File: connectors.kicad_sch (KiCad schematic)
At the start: 15 parts, among them J10 Conn_01x03_Socket, J11 Conn_01x05_Socket, J2 RJ45_RB1-125B8G1A, J6 Conn_01x04_Socket, J8 87832-1420, Q1 MMBT3904, Q2 MMBT3904

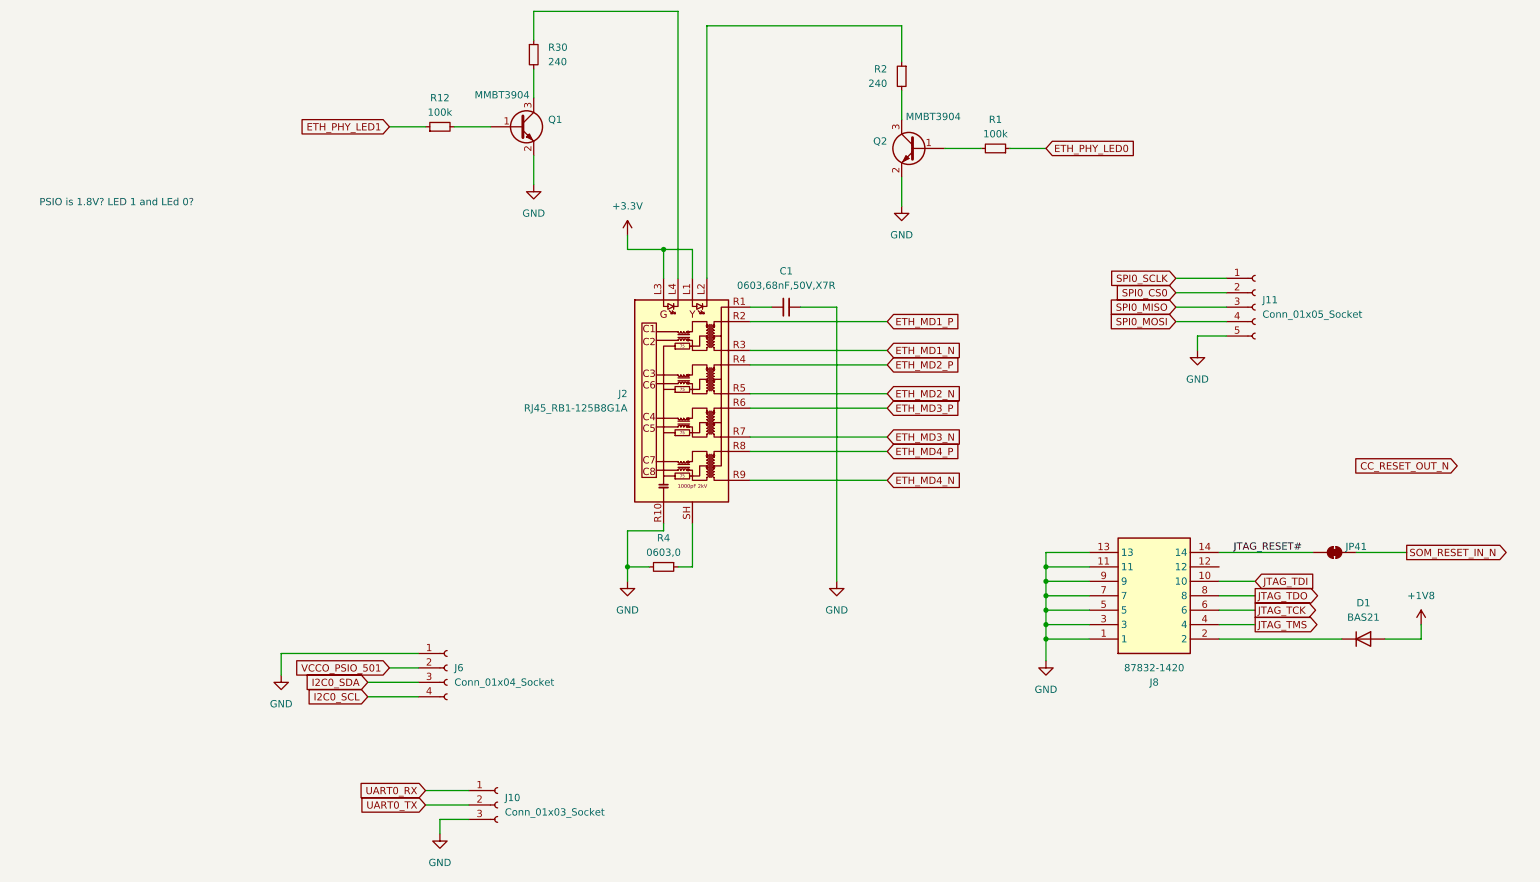
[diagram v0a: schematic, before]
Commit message: moved to 6 layers, fixing DRC issues
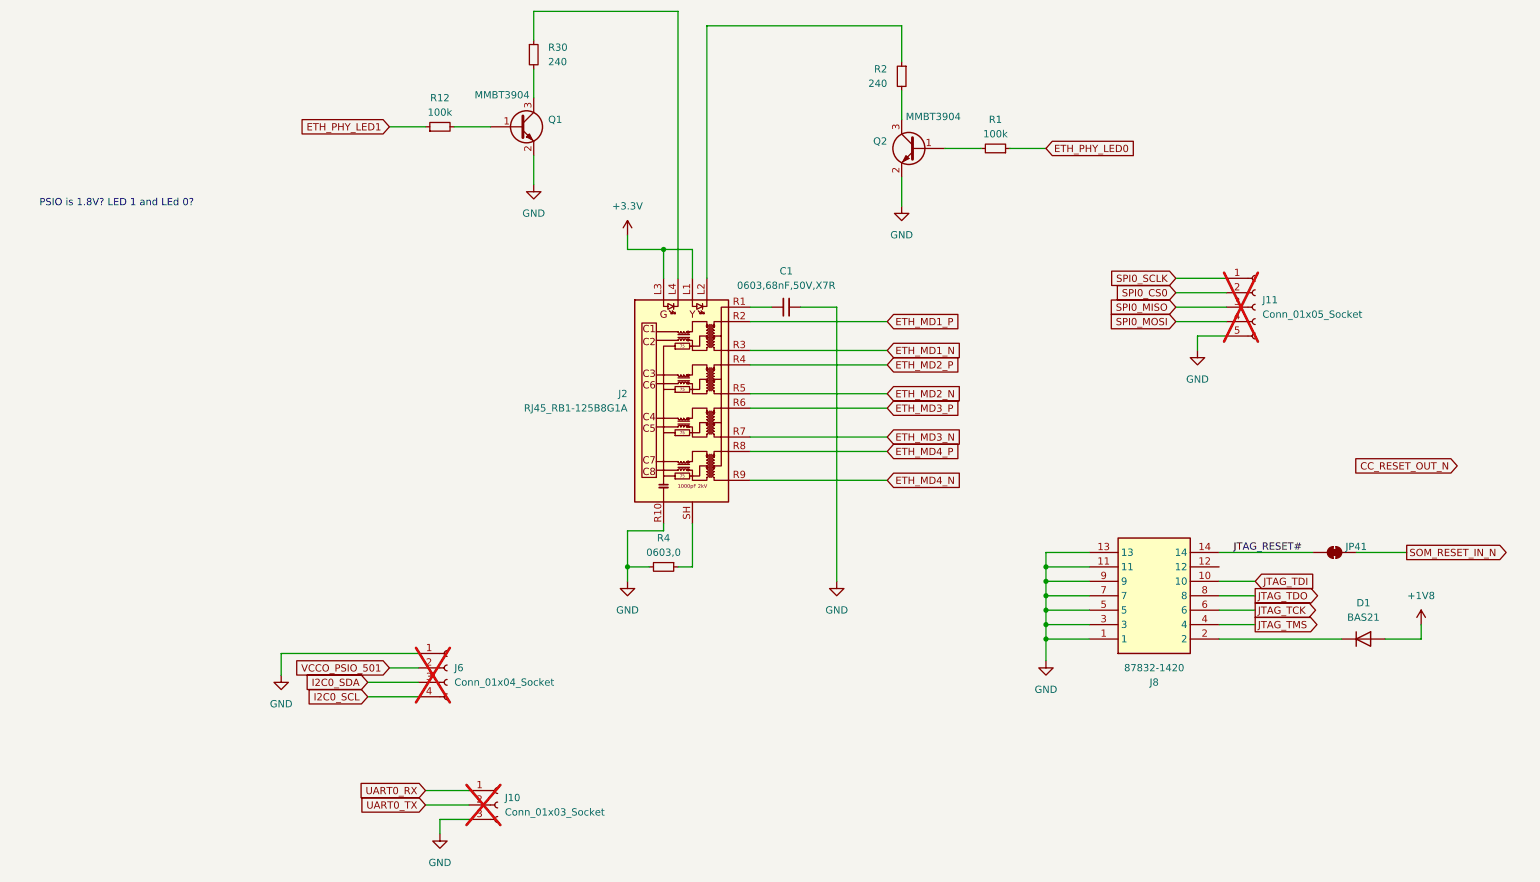
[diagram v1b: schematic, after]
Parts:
- J10, J11, J6: now not fitted
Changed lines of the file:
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@@
 		(in_bom yes)
 		(on_board yes)
-		(dnp no)
+		(dnp yes)
 		(fields_autoplaced yes)
 		(property "Reference" "J6"
@@
 		(in_bom yes)
 		(on_board yes)
-		(dnp no)
+		(dnp yes)
 		(fields_autoplaced yes)
 		(property "Reference" "J10"
@@
 		(in_bom yes)
 		(on_board yes)
-		(dnp no)
+		(dnp yes)
 		(fields_autoplaced yes)
 		(property "Reference" "J11"

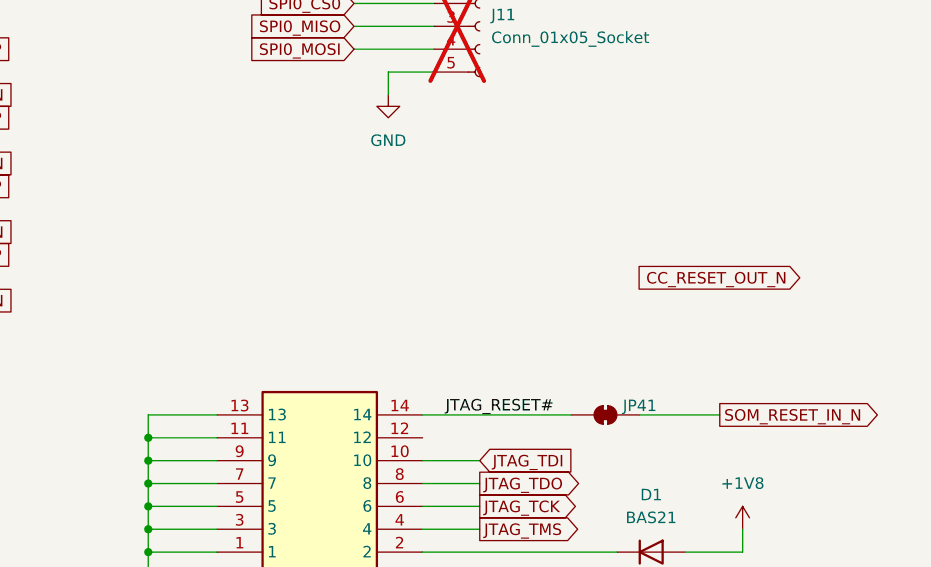
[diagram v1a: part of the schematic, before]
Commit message: moved jtag connector, added holes for all power supplies, fixed most of DRC
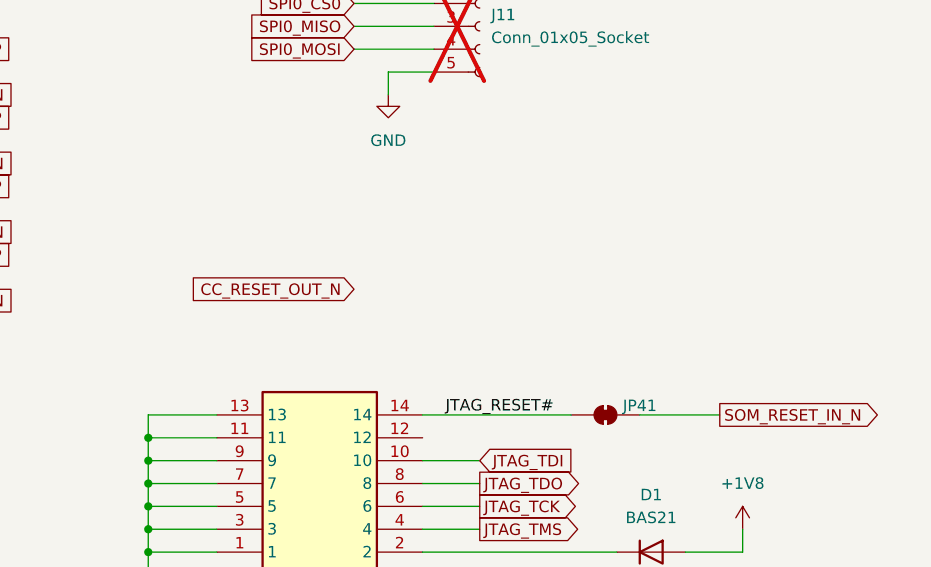
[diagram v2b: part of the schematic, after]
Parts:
- R1, R12: footprint R_0402_1005Metric -> Resistor_SMD:R_0402_1005Metric
- R2, R30: footprint R_0603_1608Metric -> Resistor_SMD:R_0603_1608Metric
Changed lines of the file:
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@@
 	(global_label "CC_RESET_OUT_N"
 		(shape input)
-		(at 231.14 119.38 180)
+		(at 181.61 120.65 180)
 		(fields_autoplaced yes)
 		(effects
@@
 		)
 		(property "Intersheetrefs" "${INTERSHEET_REFS}"
-			(at 224.8891 119.38 0)
+			(at 175.3591 120.65 0)
 			(effects
 				(font
@@
 			)
 		)
-		(property "Footprint" "R_0603_1608Metric"
+		(property "Footprint" "Resistor_SMD:R_0603_1608Metric"
 			(at 133.35 50.8 0)
 			(effects
@@
 			)
 		)
-		(property "Footprint" "R_0402_1005Metric"
+		(property "Footprint" "Resistor_SMD:R_0402_1005Metric"
 			(at 52.07 59.69 0)
 			(effects
@@
 			)
 		)
-		(property "Footprint" "R_0603_1608Metric"
+		(property "Footprint" "Resistor_SMD:R_0603_1608Metric"
 			(at 68.58 46.99 0)
 			(effects
@@
 			)
 		)
-		(property "Footprint" "R_0402_1005Metric"
+		(property "Footprint" "Resistor_SMD:R_0402_1005Metric"
 			(at 149.86 63.5 0)
 			(effects

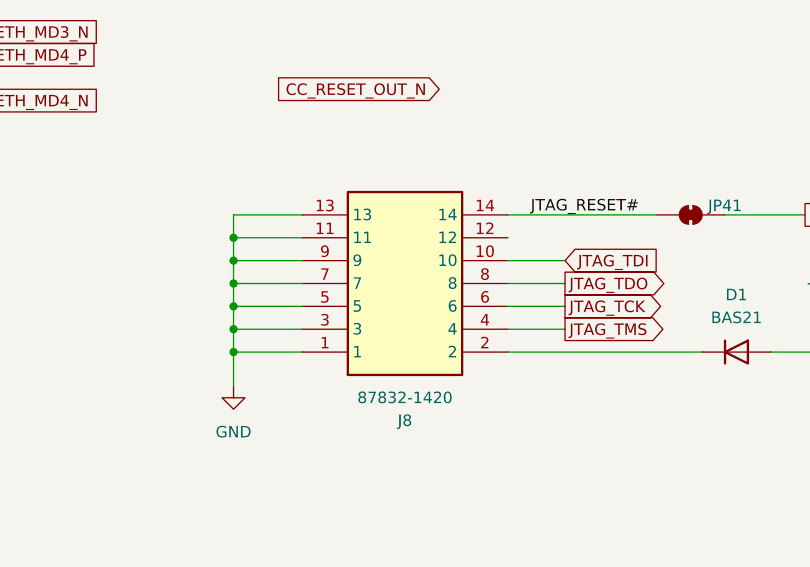
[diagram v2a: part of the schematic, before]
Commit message: marked more connectors as do not solder.
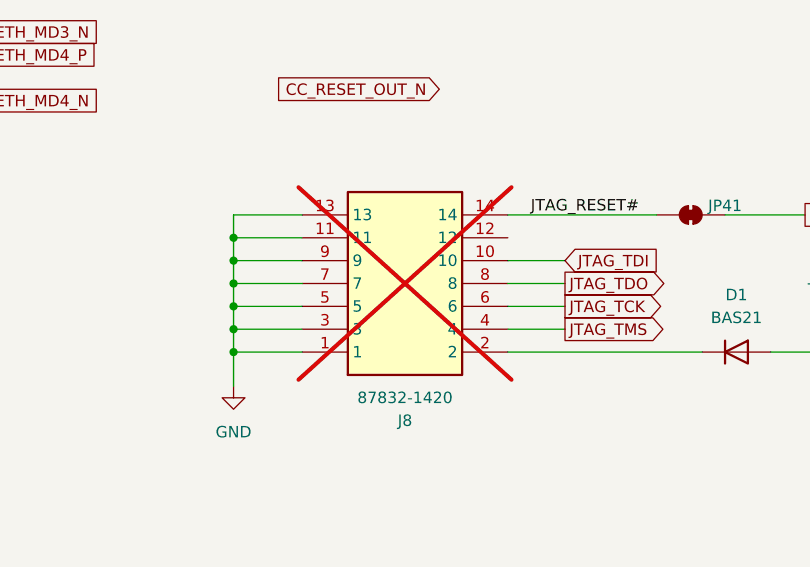
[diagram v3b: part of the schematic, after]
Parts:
- J8: now not fitted
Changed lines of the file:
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@@
 		(in_bom yes)
 		(on_board yes)
-		(dnp no)
+		(dnp yes)
 		(property "Reference" "J8"
 			(at 177.8 157.48 0)
